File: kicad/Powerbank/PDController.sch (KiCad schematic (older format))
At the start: 35 parts

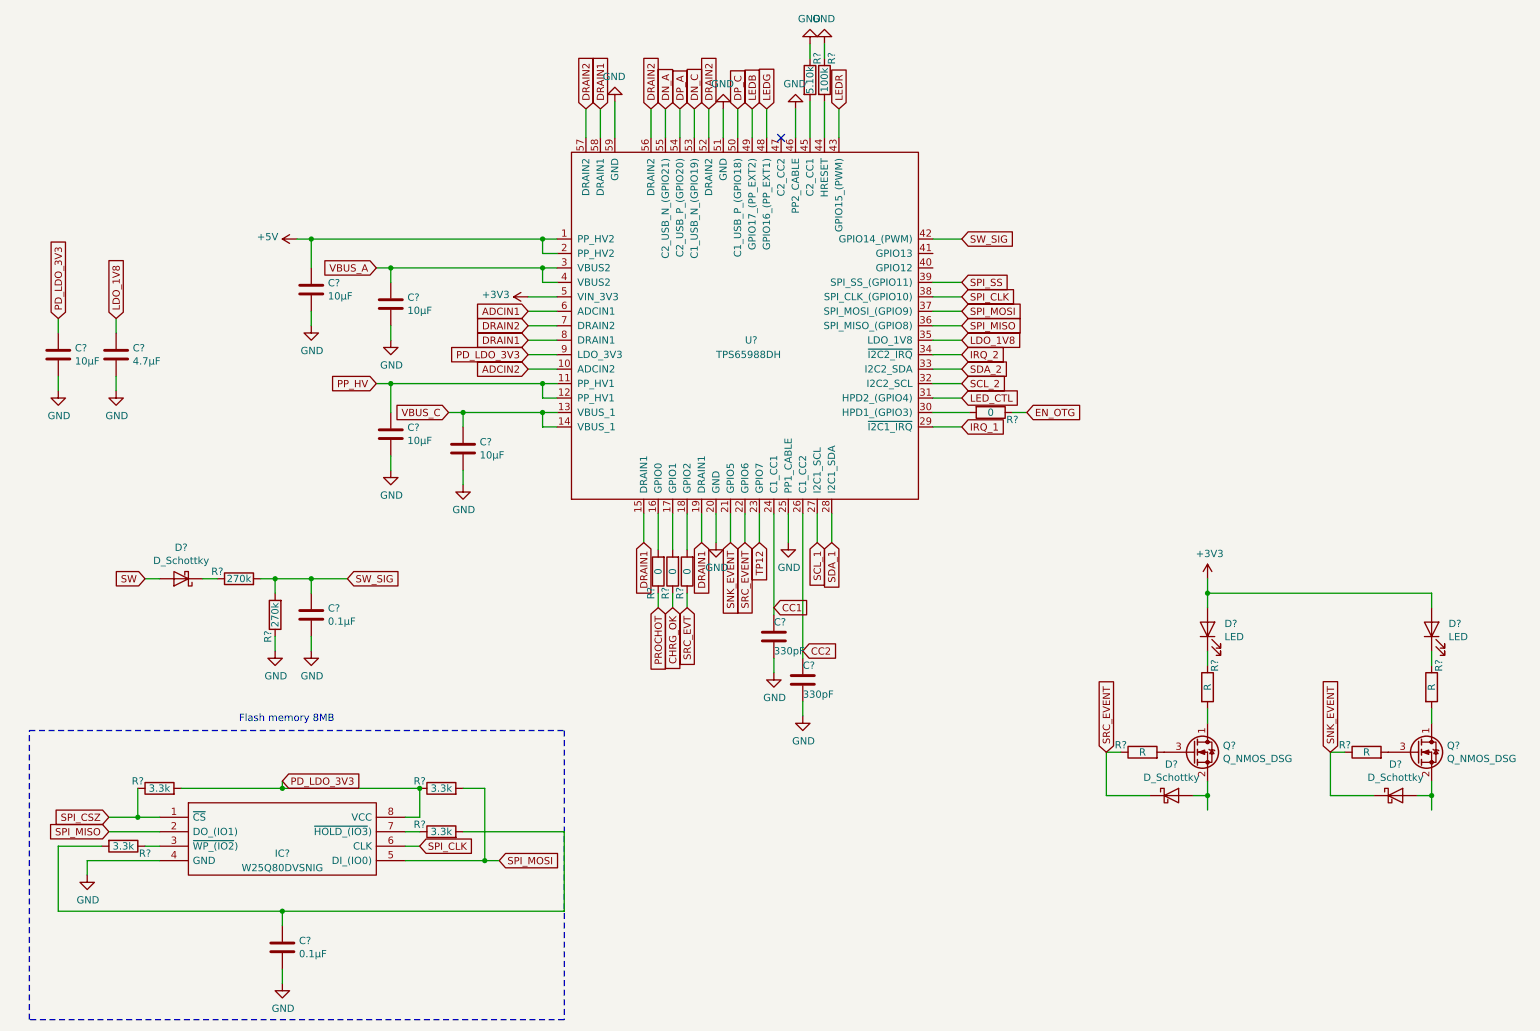
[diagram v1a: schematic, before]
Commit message: Double checked schematic towards reference design
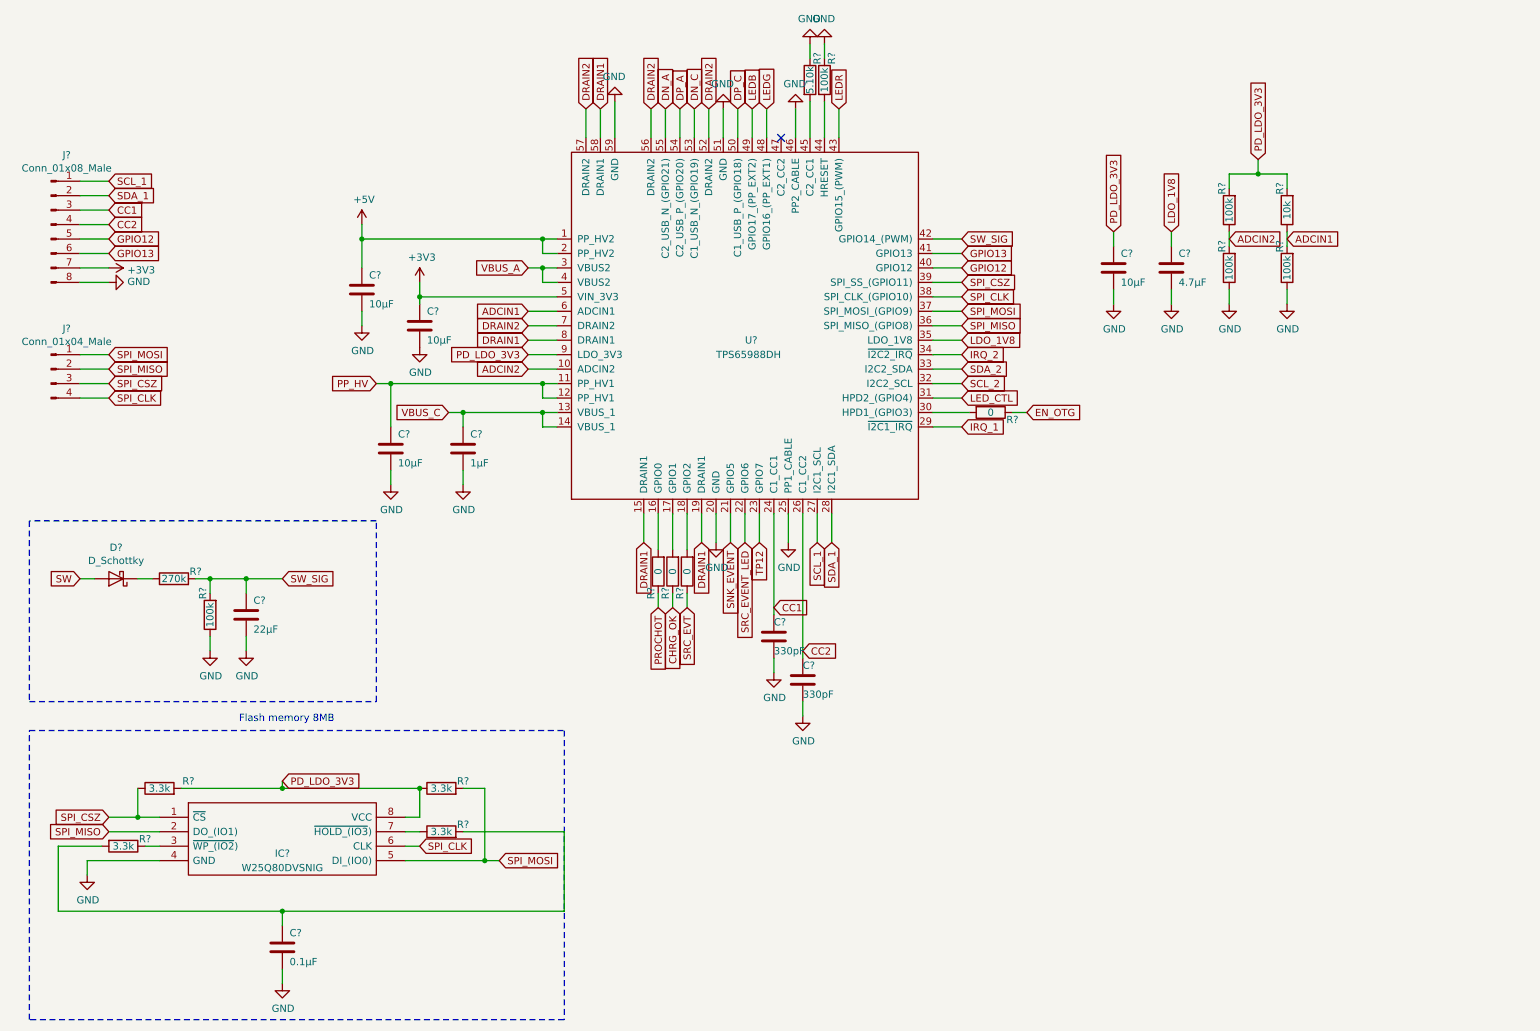
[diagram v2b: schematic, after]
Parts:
- removed C?: 10µF, symbol Device:C
- removed D? (x2): D_Schottky, symbol Device:D_Schottky
- removed D? (x2): LED, symbol Device:LED
- removed Q? (x2): Q_NMOS_DSG, symbol Device:Q_NMOS_DSG
- removed R? (x4): R, symbol Device:R
- added C?: 10µF, symbol Device:C
- added J?: Conn_01x08_Male, symbol Connector:Conn_01x08_Male
- added J?: Conn_01x04_Male, symbol Connector:Conn_01x04_Male
- added R? (x3): 100k, symbol Device:R
- added R?: 10k, symbol Device:R
- C?: value 0.1µF -> 22µF
- C?: value 10µF -> 1µF
- R?: value 270k -> 100k
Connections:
- net SPI_SS is gone; now on net SPI_CSZ: U?.39 (SPI_SS_(GPIO11))
- net +3V3: now also C?.1, J?.7 (Pin_7)
- net ADCIN1: now also R?.1, R?.2
- net ADCIN2: now also R?.1, R?.2
- net CC1: now also J?.3 (Pin_3)
- net CC2: now also J?.4 (Pin_4)
- net GND: now also C?.2, J?.8 (Pin_8), R?.1, R?.1
- net PD_LDO_3V3: now also R?.2, R?.2
- net SCL_1: now also J?.1 (Pin_1)
- net SDA_1: now also J?.2 (Pin_2)
- net SPI_CLK: now also J?.4 (Pin_4)
- net SPI_CSZ: now also J?.3 (Pin_3)
- net SPI_MISO: now also J?.2 (Pin_2)
- net SPI_MOSI: now also J?.1 (Pin_1)
- net GPIO12: now reaches U?.40 (GPIO12)
- net GPIO12: now also J?.5 (Pin_5)
- net GPIO13: now reaches U?.41 (GPIO13)
- net GPIO13: now also J?.6 (Pin_6)
- net SRC_EVENT renamed SRC_EVENT_LED
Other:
- moved on the sheet: C?, D?, R?

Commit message: Updated for PCB
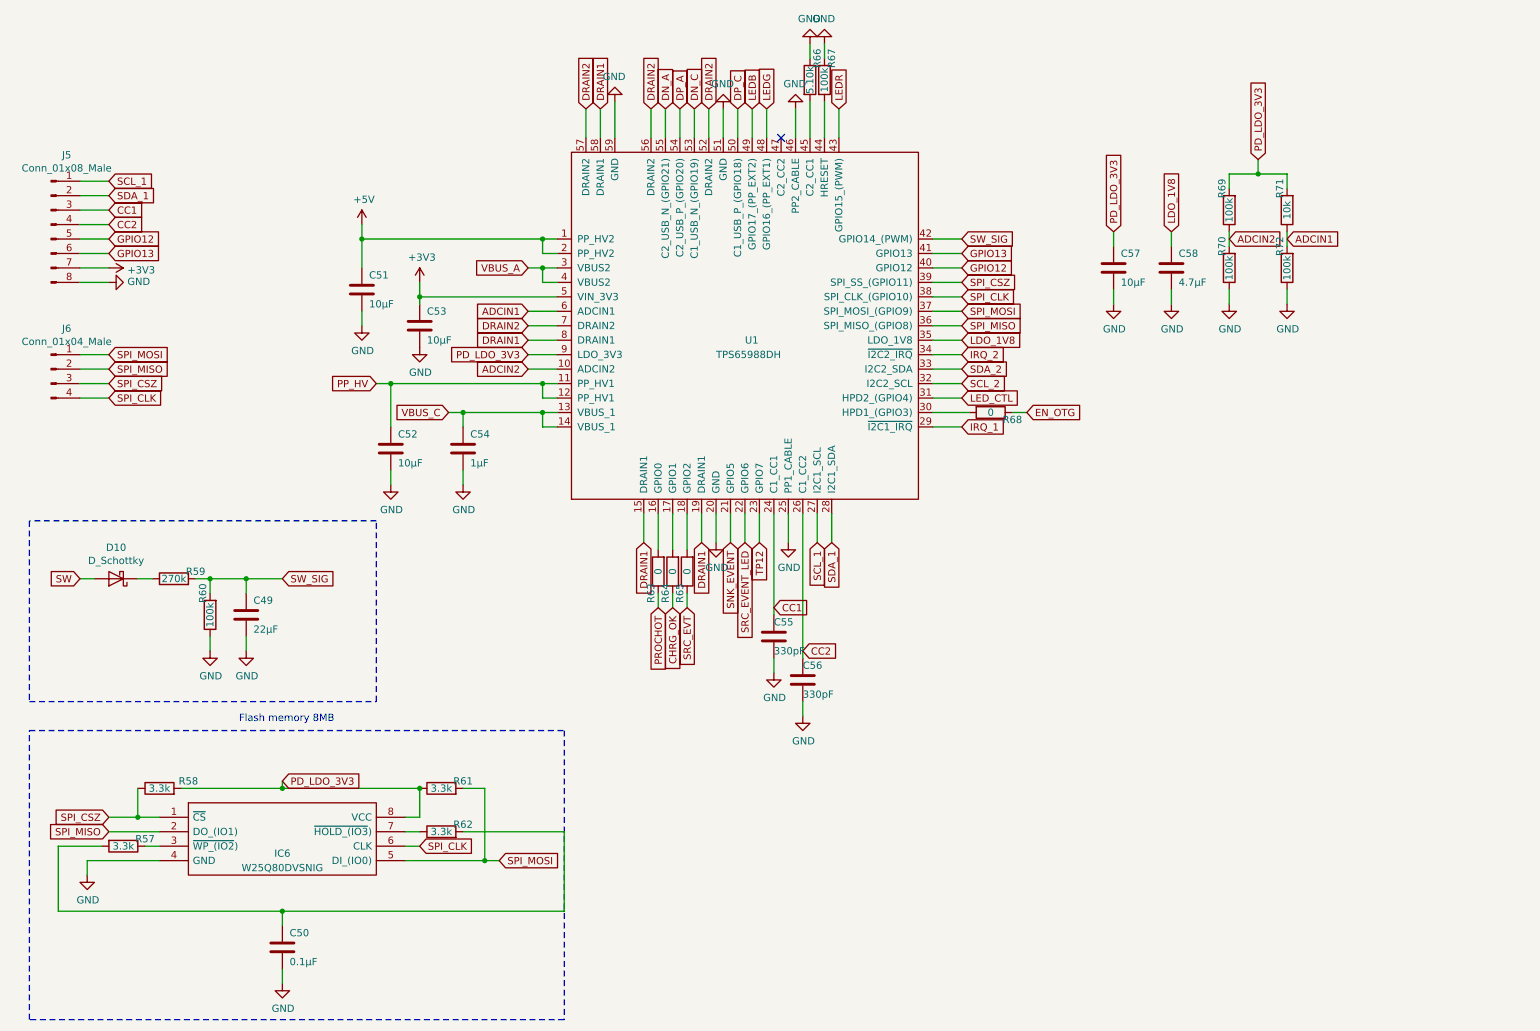
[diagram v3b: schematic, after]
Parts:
- C49: renamed from C?; footprint (none) -> Capacitor_SMD:C_0805_2012Metric
- C50, C51, C52, C53, C54, C55, C56, C57, C58: renamed from C?; footprint (none) -> Capacitor_SMD:C_0603_1608Metric
- IC6: renamed from IC?; footprint SOIC127P600X175-8N -> Powerbank:SOIC127P600X175-8N
- J5: renamed from J?; footprint (none) -> Connector_JST:JST_ZE_S08B-ZESK-2D_1x08_P1.50mm_Horizontal
- J6: renamed from J?; footprint (none) -> Connector_JST:JST_ZE_BM04B-ZESS-TBT_1x04-1MP_P1.50mm_Vertical
- R57, R58, R59, R60, R61, R62, R63, R64, R65, R66, R67, R68, R69, R70, R71, R72: renamed from R?; footprint (none) -> Resistor_SMD:R_0603_1608Metric
- gave numbers to parts that had none: 2

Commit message: Added footprint for all, moved to a first attempt for routing
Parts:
- D10: footprint (none) -> Diode_SMD:D_SOD-523
- J5: footprint Connector_JST:JST_ZE_S08B-ZESK-2D_1x08_P1.50mm_Horizontal -> Connector_PinHeader_1.27mm:PinHeader_2x04_P1.27mm_Vertical
- J6: footprint Connector_JST:JST_ZE_BM04B-ZESS-TBT_1x04-1MP_P1.50mm_Vertical -> Connector_PinHeader_1.27mm:PinHeader_2x02_P1.27mm_Vertical
- U1: footprint (none) -> Powerbank:QFN-56_7x7_Pitch0.4mm
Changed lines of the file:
@@
 F 0 "D10" H 1250 4484 50  0000 C CNN
 F 1 "D_Schottky" H 1250 4575 50  0000 C CNN
-F 2 "" H 1250 4700 50  0001 C CNN
+F 2 "Diode_SMD:D_SOD-523" H 1250 4700 50  0001 C CNN
 F 3 "~" H 1250 4700 50  0001 C CNN
 	1    1250 4700
@@
 F 0 "U1" H 5600 3150 50  0000 L CNN
 F 1 "TPS65988DH" H 5400 3050 50  0000 L CNN
-F 2 "" H 5600 3100 50  0001 C CNN
+F 2 "Powerbank:QFN-56_7x7_Pitch0.4mm" H 5600 3100 50  0001 C CNN
 F 3 "" H 5600 3100 50  0001 C CNN
 	1    5600 3100
@@
 F 0 "J5" H 908 2731 50  0000 C CNN
 F 1 "Conn_01x08_Male" H 908 2640 50  0000 C CNN
-F 2 "Connector_JST:JST_ZE_S08B-ZESK-2D_1x08_P1.50mm_Horizontal" H 800 2250 50  0001 C CNN
+F 2 "Connector_PinHeader_1.27mm:PinHeader_2x04_P1.27mm_Vertical" H 800 2250 50  0001 C CNN
 F 3 "~" H 800 2250 50  0001 C CNN
 	1    800  2250
@@
 F 0 "J6" H 908 3531 50  0000 C CNN
 F 1 "Conn_01x04_Male" H 908 3440 50  0000 C CNN
-F 2 "Connector_JST:JST_ZE_BM04B-ZESS-TBT_1x04-1MP_P1.50mm_Vertical" H 800 3250 50  0001 C CNN
+F 2 "Connector_PinHeader_1.27mm:PinHeader_2x02_P1.27mm_Vertical" H 800 3250 50  0001 C CNN
 F 3 "~" H 800 3250 50  0001 C CNN
 	1    800  3250

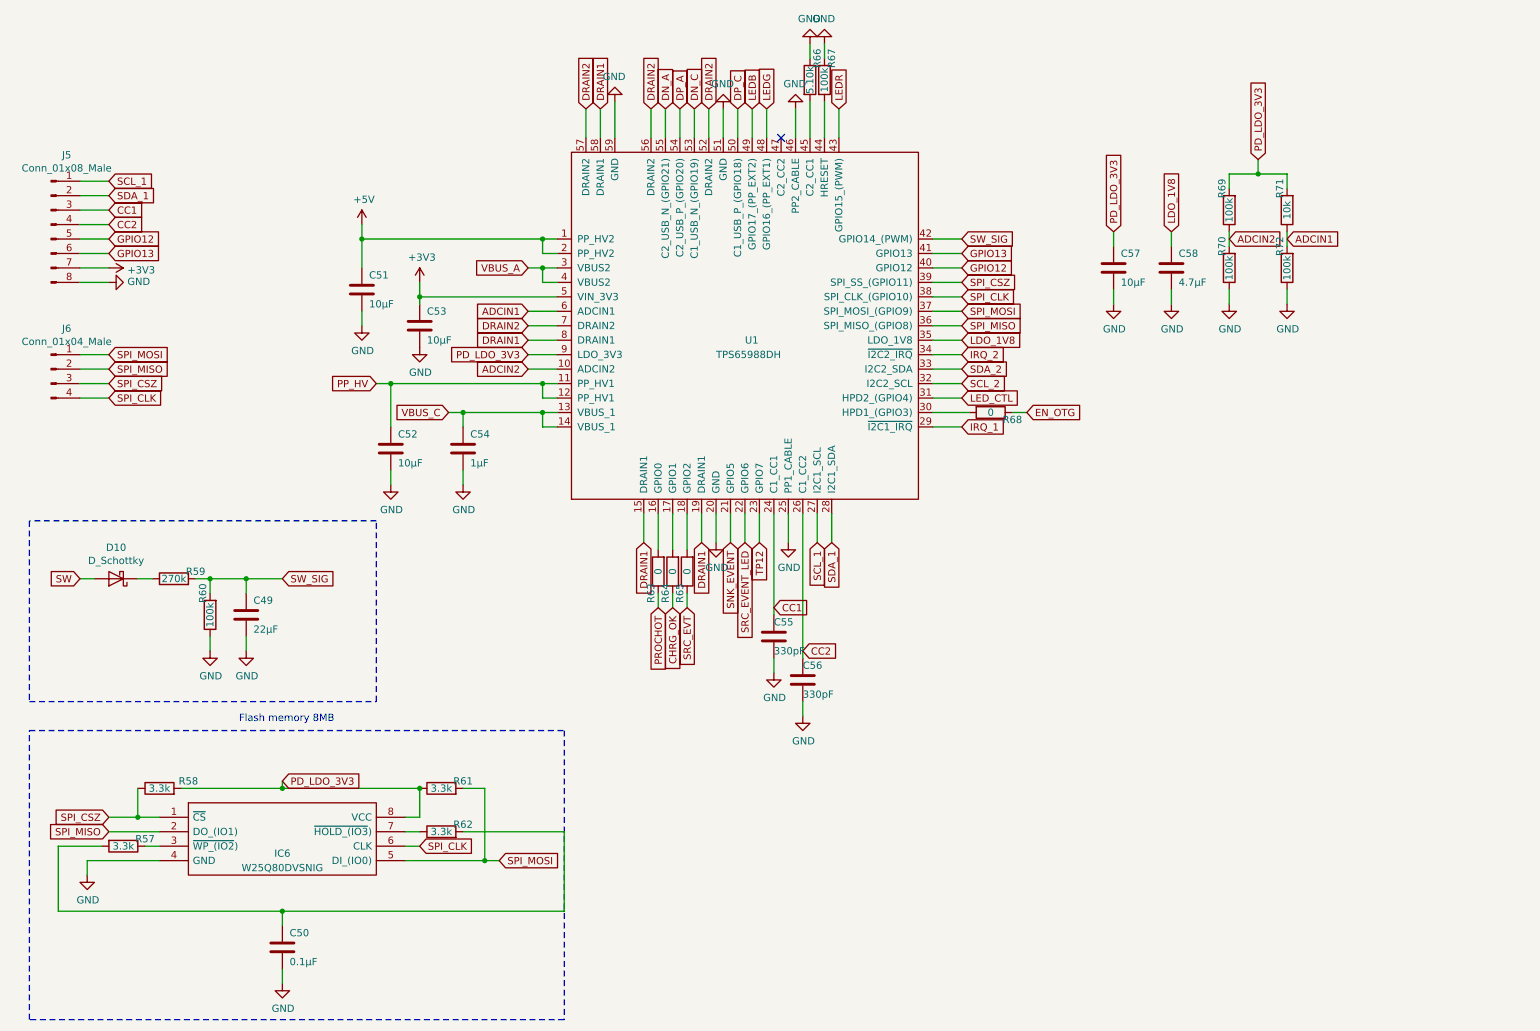
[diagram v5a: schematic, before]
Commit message: Updated layout in schematic for nicer look
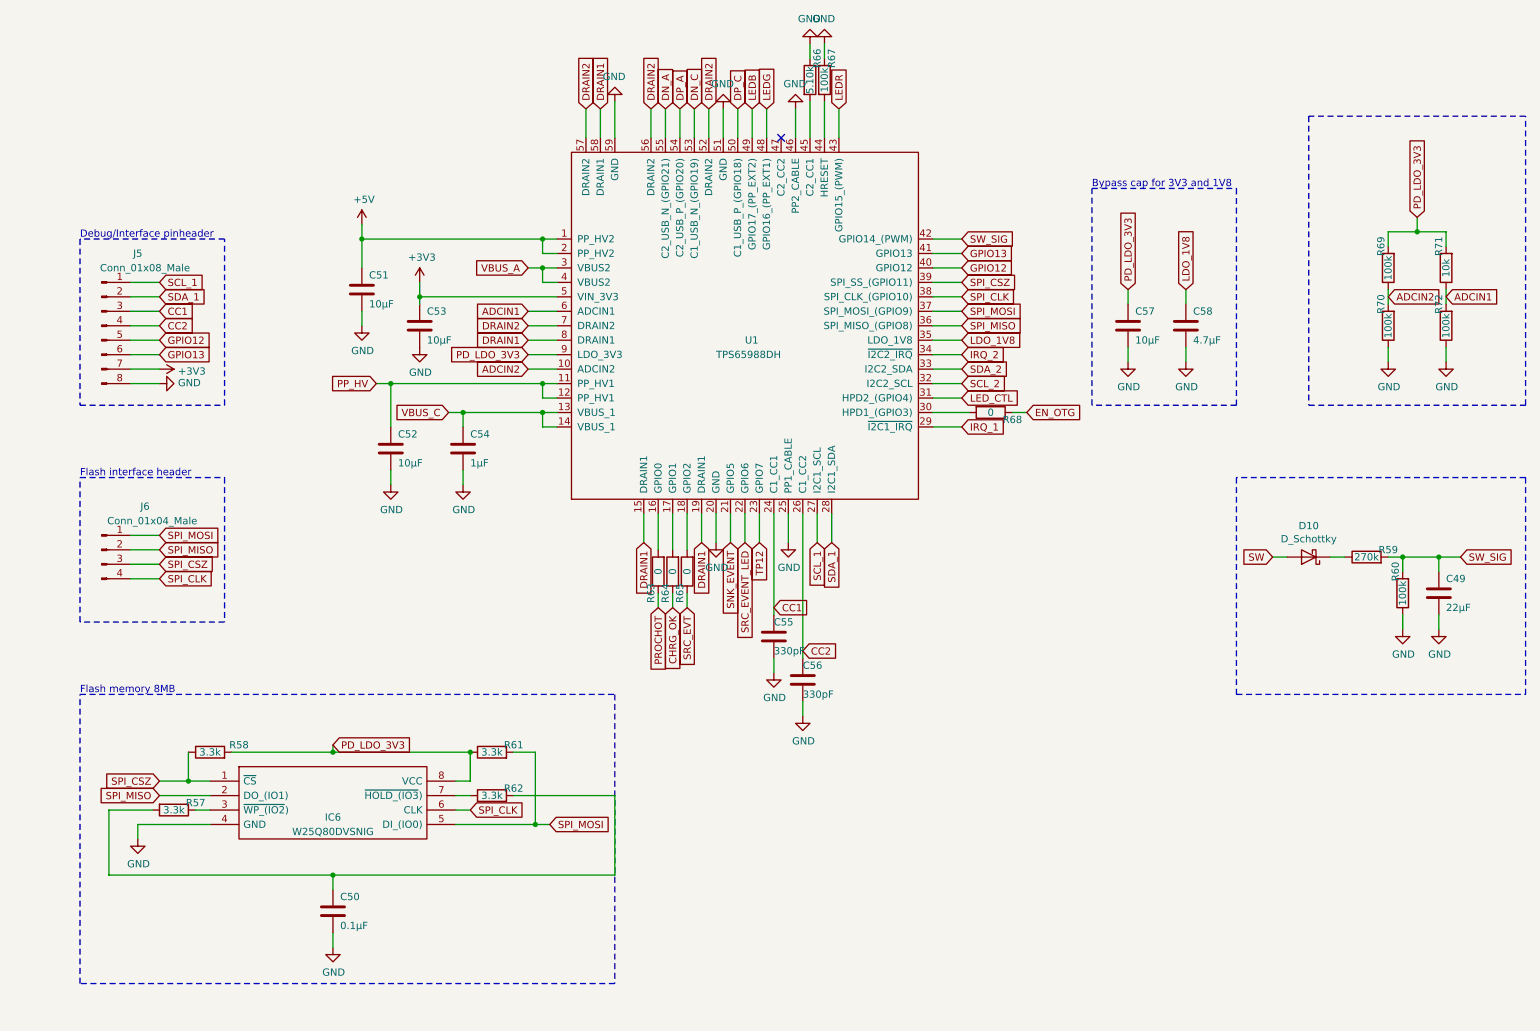
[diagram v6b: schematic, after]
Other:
- note added: "Bypass cap for 3V3 and 1V8"
- note added: "Debug/Interface pinheader"
- note added: "Flash interface header"
- moved on the sheet: C49, C50, C57, C58, D10, IC6, J5, J6, R57, R58, R59, R60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
